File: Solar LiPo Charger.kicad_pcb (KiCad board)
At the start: 2 copper layers, 50.2 x 34.3 mm, 40 parts, among them J1 Barrel_Jack, Q1 DMN3404L-7, U1 bq24650

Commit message: Rev2B Layout
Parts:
- removed MT1, MT2, MT3: , MountingHole:MountingHole_2.7mm_M2.5
- D4: footprint digikey-footprints:SOT-23-3 -> digikey-footprints:SOT-23-3-MC2
- moved C8 13.0 mm to (147.3, 91.4)
- moved C12 12.0 mm to (144.8, 91.7), turned to 270 degrees
- moved C14 11.9 mm to (134.1, 91.9), turned to 270 degrees
- moved C6 11.6 mm to (127.8, 79.2), turned to 270 degrees
- moved C11 11.0 mm to (137.2, 82.3), turned to 180 degrees
- moved D4 10.7 mm to (137.2, 79.3)
- moved C9 8.27 mm to (137.7, 86.1), turned to 270 degrees
- moved C10 7.64 mm to (140.2, 86.1), turned to 90 degrees
- moved C13 7.60 mm to (141.7, 91.7), turned to 270 degrees
- moved R12 6.88 mm to (136.5, 91.9), turned to 270 degrees
- moved R13 6.45 mm to (138.9, 91.9)
- moved C1 5.36 mm to (123.7, 86.6)
- moved R11 3.81 mm to (141.0, 80.5)
- moved L1 3.32 mm to (137.7, 72.6)
- moved C7 3.07 mm to (130.8, 89.4)
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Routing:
- net BTST: track 46.7 -> 16.6 mm, vias 4 -> 0
- net SRP: track 39.6 -> 21.3 mm, vias 2 -> 0
- net GND: track 11.0 -> 0.00 mm, vias 4 -> 0
- net Net-(C6-Pad2): track 12.1 -> 3.61 mm, vias 2 -> 0
- net Net-(C11-Pad2): track 16.0 -> 8.87 mm, vias 4 -> 0
- net VFB: track 19.9 -> 13.7 mm, vias 3 -> 0
- net SRN: track 37.4 -> 42.0 mm
- net Net-(C1-Pad1): track 7.28 -> 2.99 mm, vias 2 -> 0
- net Net-(C7-Pad1): track 6.74 -> 3.65 mm, vias 2 -> 0
- net Net-(R8-Pad1): track 8.09 -> 5.36 mm
- net TS: track 13.1 -> 10.5 mm
- net Net-(D2-Pad1): track 12.1 -> 10.0 mm, vias 2 -> 0
- net Net-(Q1-Pad2): track 4.45 -> 2.36 mm
- net Net-(C3-Pad1): track 27.1 -> 25.1 mm
- net Net-(R7-Pad2): track 4.17 -> 2.67 mm
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- removed copper zone on F.Cu, net SRP

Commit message: Rev2B Final
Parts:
- added MT1: MountingHole_2.2mm_M2_Pad, MountingHole:MountingHole_2.2mm_M2_Pad, F.Cu at (107.7, 98.0)
- added MT2: MountingHole_2.2mm_M2_Pad, MountingHole:MountingHole_2.2mm_M2_Pad, F.Cu at (150.9, 98.3)
- added MT3: MountingHole_2.2mm_M2_Pad, MountingHole:MountingHole_2.2mm_M2_Pad, F.Cu at (151.1, 70.4)
- D4: footprint digikey-footprints:SOT-23-3-MC2 -> Diode_SMD:D_SOT-23_ANK-MC
- Q1, Q2: footprint digikey-footprints:SOT-23-3 -> Diode_SMD:D_SOT-23-Q
- moved C1 3.56 mm to (123.7, 90.2)
- moved R1 2.79 mm to (118.3, 89.9)
- moved R3 2.24 mm to (123.2, 87.4)
- moved R2 2.16 mm to (118.4, 87.4)
- moved R11 1.98 mm to (142.5, 81.8)
- moved C12 0.51 mm to (144.8, 92.2)
- moved C13 0.51 mm to (141.7, 92.2)
- moved C3 0.51 mm to (123.4, 74.2)
- moved C5 0.51 mm to (123.7, 79.2)
- moved D3 0.51 mm to (122.7, 95.1)
- moved D4 0.51 mm to (137.2, 79.8)
- moved J1 0.51 mm to (118.7, 74.2)
- moved J2 0.51 mm to (149.7, 81.5)
- moved R4 0.51 mm to (124.7, 84.3)
- moved R5 0.51 mm to (118.3, 92.5)
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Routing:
- net GND: track 0.00 -> 7.29 mm, vias 0 -> 5
- net BTST: track 16.6 -> 21.7 mm
- net SRN: track 42.0 -> 39.1 mm
- net MPPSET: track 13.6 -> 10.9 mm, vias 1 -> 0
- net Vsolar: track 23.4 -> 24.6 mm
- net SRP: track 21.3 -> 22.2 mm
- net Net-(D2-Pad1): track 10.0 -> 10.9 mm
- net VFB: track 13.7 -> 14.5 mm
- added copper zone on F.Cu, net SRN
- added copper zone on F.Cu, net SRP

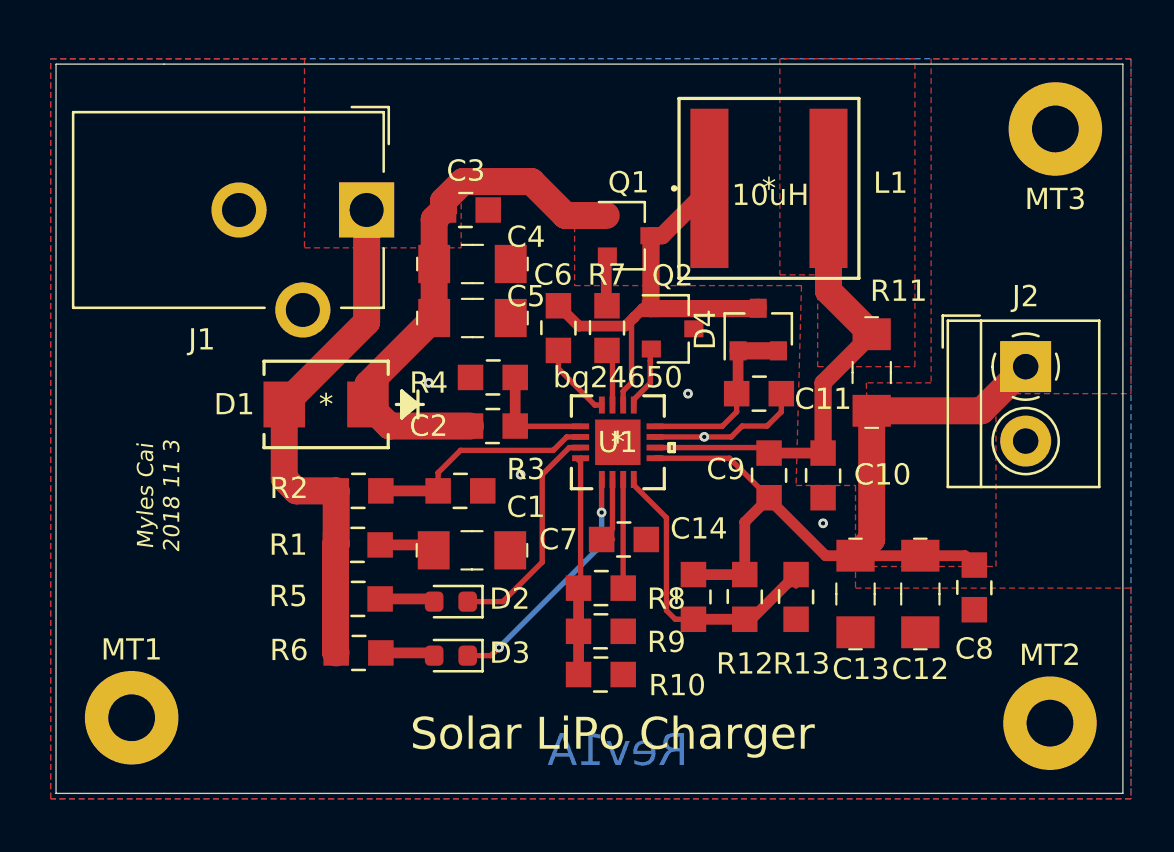
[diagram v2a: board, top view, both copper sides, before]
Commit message: rounded edges
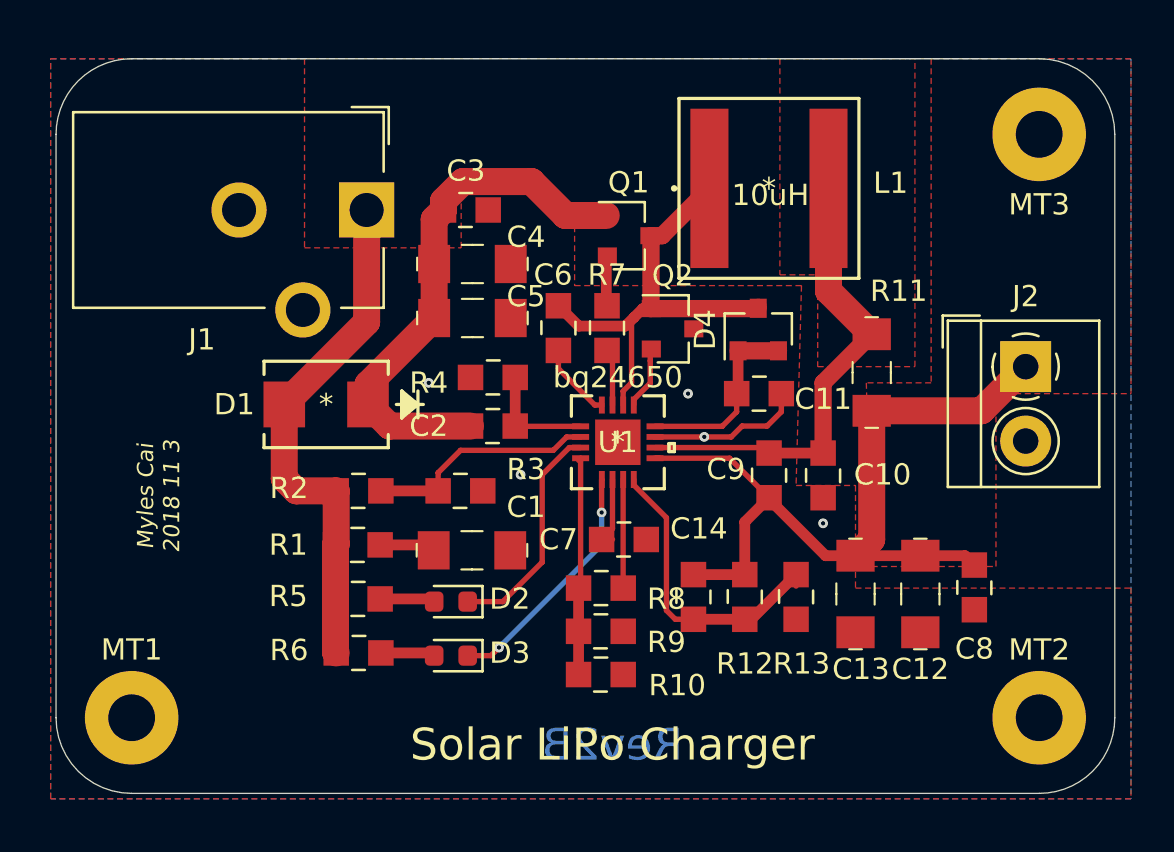
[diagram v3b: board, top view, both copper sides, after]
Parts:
- moved MT3 0.80 mm to (150.4, 70.6)
- moved MT2 0.57 mm to (150.4, 98.0)
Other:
- board size 50.2 x 34.3 mm -> 49.8 x 34.5 mm
- board text added: "Rev2B"
- board text removed: "Rev1A"

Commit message: moved input filt
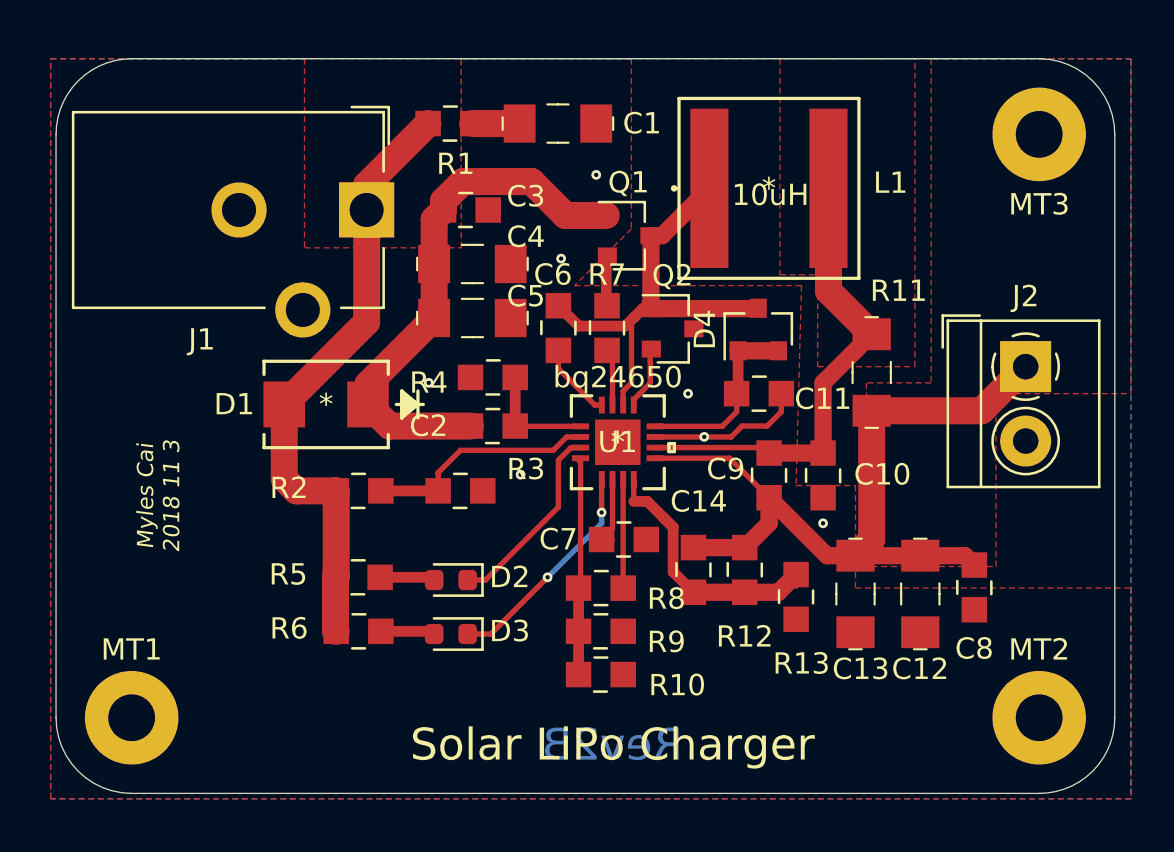
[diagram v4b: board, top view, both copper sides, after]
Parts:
- moved C1 20.5 mm to (127.7, 70.1)
- moved R1 20.3 mm to (122.7, 70.1)
- moved C14 1.27 mm to (134.1, 91.1)
- moved R12 1.27 mm to (136.5, 91.1)
- moved D2 1.02 mm to (122.7, 91.6)
- moved D3 1.02 mm to (122.7, 94.1)
- moved R5 1.02 mm to (118.3, 91.4)
- moved R6 1.02 mm to (118.4, 94.0)
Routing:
- net Vsolar: track 24.6 -> 28.8 mm
- net Net-(D2-Pad1): track 10.9 -> 9.18 mm
- net SRN: track 39.1 -> 37.9 mm
- net VFB: track 14.5 -> 13.4 mm
- net Net-(D3-Pad1): track 11.5 -> 10.5 mm
- net GND: vias 5 -> 7
